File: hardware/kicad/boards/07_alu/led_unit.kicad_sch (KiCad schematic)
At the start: 120 parts

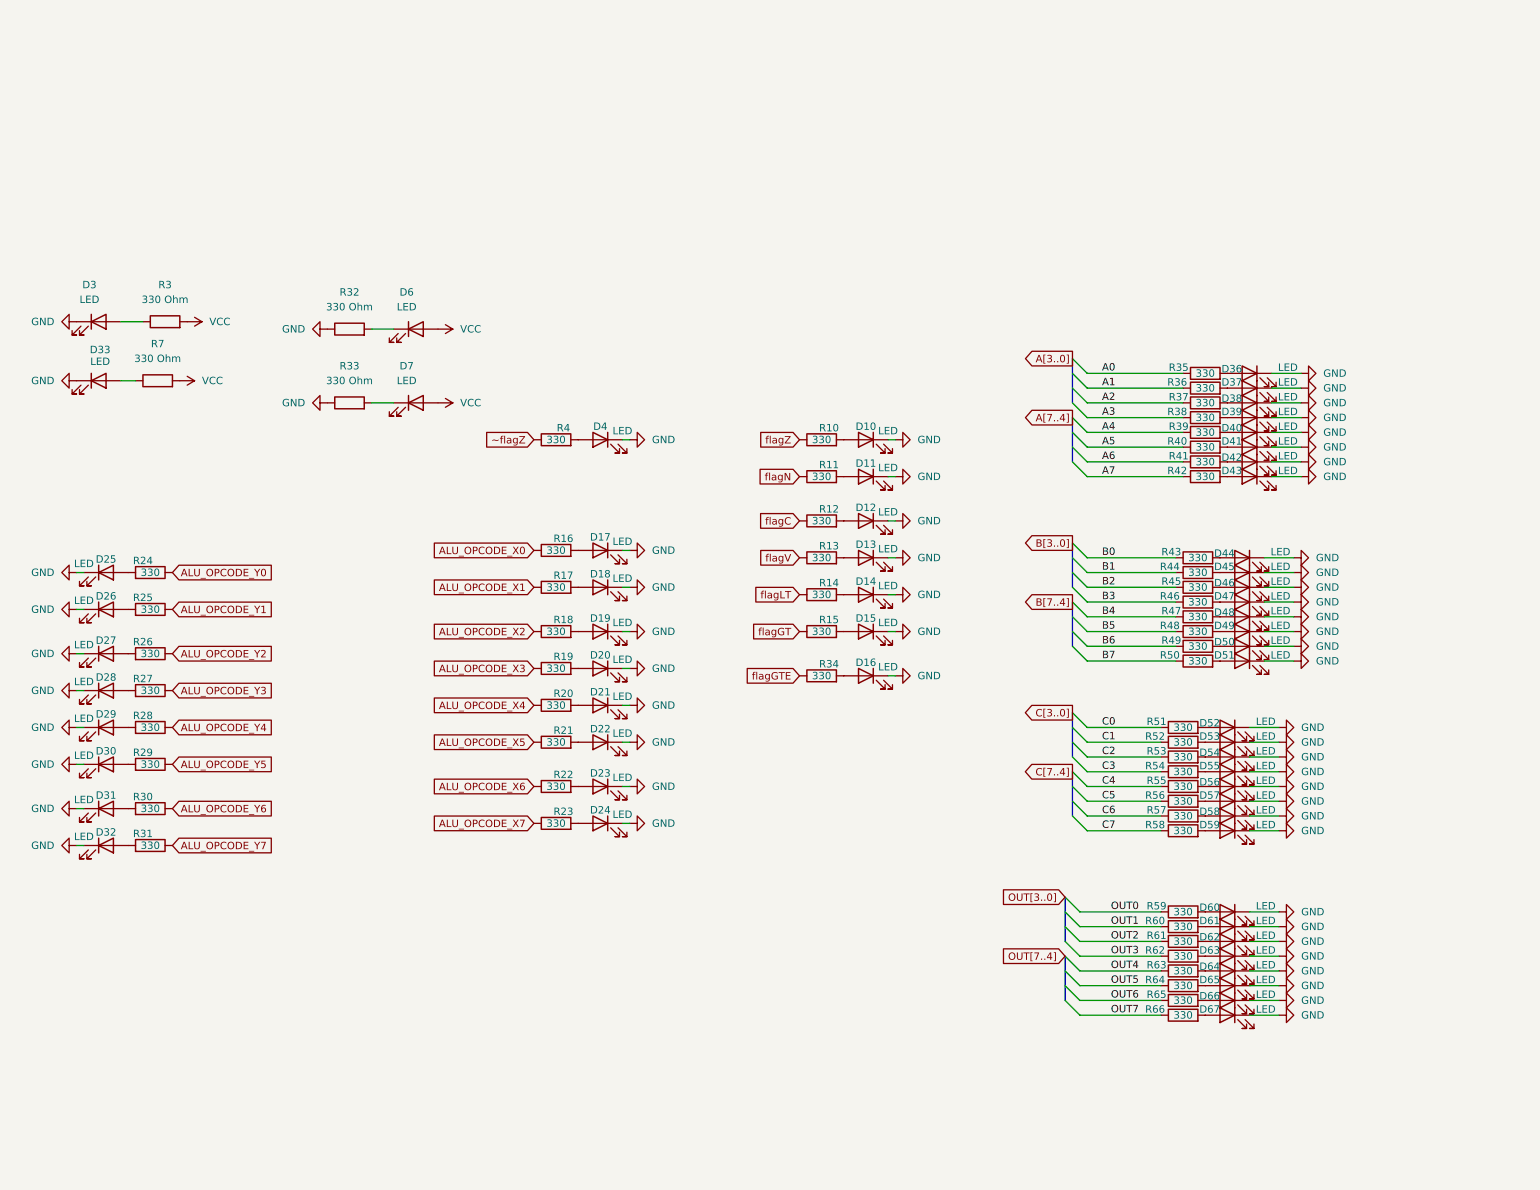
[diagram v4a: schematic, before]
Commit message: fix: replaced with resistor array/network over individual components
fix #5
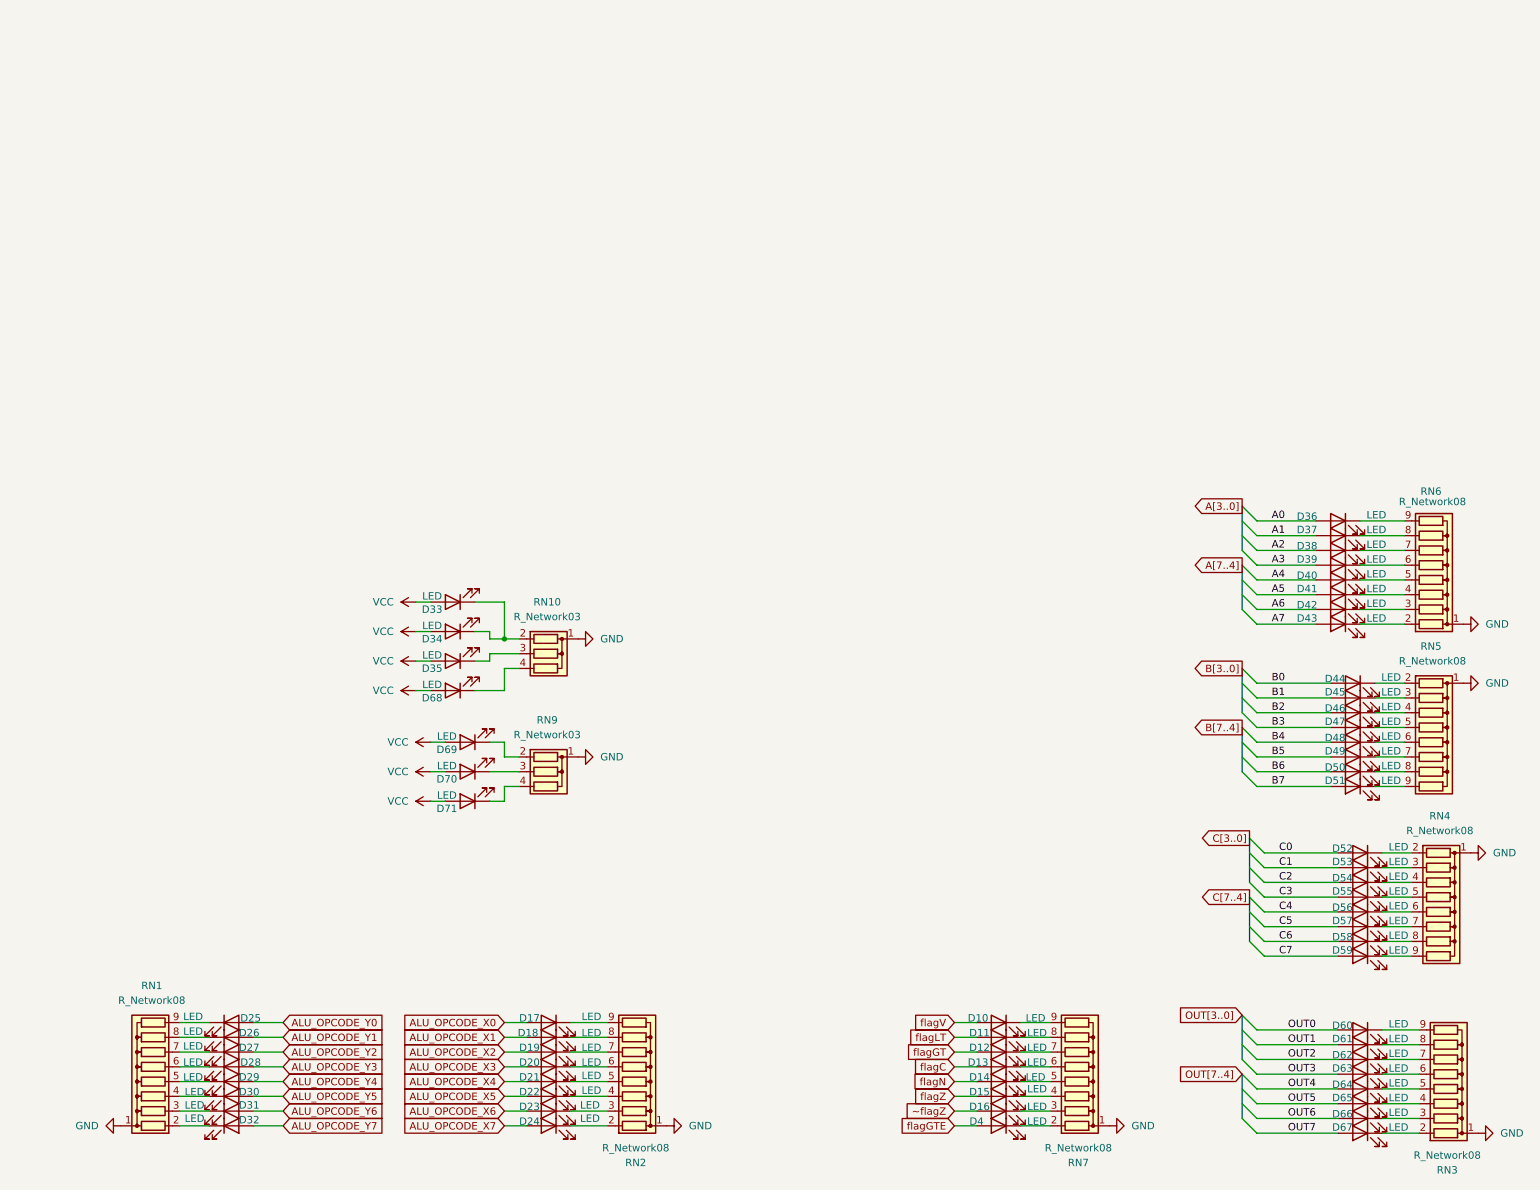
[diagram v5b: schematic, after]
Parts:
- removed D3, D6, D7: LED, LED_SMD:LED_0805_2012Metric, symbol Device:LED
- removed R10, R11, R12, R13, R14, R15, R16, R17, R18, R19, R20, R21, R22, R23, R24, R25, R26, R27, R28, R29, R30, R31, R34, R35, R36, R37, R38, R39, R4, R40, R41, R42, R43, R44, R45, R46, R47, R48, R49, R50, R51, R52, R53, R54, R55, R56, R57, R58, R59, R60, R61, R62, R63, R64, R65, R66: 330, Resistor_SMD:R_0603_1608Metric, symbol Device:R
- removed R3, R32, R33, R7: 330 Ohm, Resistor_SMD:R_0603_1608Metric, symbol Device:R
- added D34, D35, D68, D69, D70, D71: LED, LED_SMD:LED_0805_2012Metric, symbol Device:LED
- added RN1, RN2, RN3, RN4, RN5, RN6, RN7: R_Network08, Resistor_THT:R_Array_SIP9, symbol Device:R_Network08
- added RN10, RN9: R_Network03, Resistor_THT:R_Array_SIP4, symbol Device:R_Network03
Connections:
- net A0: now also D36.2 (A)
- net A1: now also D37.2 (A)
- net A2: now also D38.2 (A)
- net A3: now also D39.2 (A)
- net A4: now also D40.2 (A)
- net A5: now also D41.2 (A)
- net A6: now also D42.2 (A)
- net A7: now also D43.2 (A)
- net ALU_OPCODE_X0: now also D17.2 (A)
- net ALU_OPCODE_X1: now also D18.2 (A)
- net ALU_OPCODE_X2: now also D19.2 (A)
- net ALU_OPCODE_X3: now also D20.2 (A)
- net ALU_OPCODE_X4: now also D21.2 (A)
- net ALU_OPCODE_X5: now also D22.2 (A)
- net ALU_OPCODE_X6: now also D23.2 (A)
- net ALU_OPCODE_X7: now also D24.2 (A)
- net ALU_OPCODE_Y0: now also D25.2 (A)
- net ALU_OPCODE_Y1: now also D26.2 (A)
- net ALU_OPCODE_Y2: now also D27.2 (A)
- net ALU_OPCODE_Y3: now also D28.2 (A)
- net ALU_OPCODE_Y4: now also D29.2 (A)
- net ALU_OPCODE_Y5: now also D30.2 (A)
- net ALU_OPCODE_Y6: now also D31.2 (A)
- net ALU_OPCODE_Y7: now also D32.2 (A)
- net B0: now also D44.2 (A)
- net B1: now also D45.2 (A)
- net B2: now also D46.2 (A)
- net B3: now also D47.2 (A)
- net B4: now also D48.2 (A)
- net B5: now also D49.2 (A)
- net B6: now also D50.2 (A)
- net B7: now also D51.2 (A)
- net C0: now also D52.2 (A)
- net C1: now also D53.2 (A)
- net C2: now also D54.2 (A)
- net C3: now also D55.2 (A)
- net C4: now also D56.2 (A)
- net C5: now also D57.2 (A)
- net C6: now also D58.2 (A)
- net C7: now also D59.2 (A)
- net GND: now also RN1.1 (common), RN10.1 (common), RN2.1 (common), RN3.1 (common), RN4.1 (common), RN5.1 (common), RN6.1 (common), RN7.1 (common), RN9.1 (common); no longer D10.1 (K), D11.1 (K), D12.1 (K), D13.1 (K), D14.1 (K), D15.1 (K), D16.1 (K), D17.1 (K), D18.1 (K), D19.1 (K), D20.1 (K), D21.1 (K), D22.1 (K), D23.1 (K), D24.1 (K), D25.1 (K), D26.1 (K), D27.1 (K), D28.1 (K), D29.1 (K), D30.1 (K), D31.1 (K), D32.1 (K), D33.1 (K), D36.1 (K), D37.1 (K), D38.1 (K), D39.1 (K), D4.1 (K), D40.1 (K), D41.1 (K), D42.1 (K), D43.1 (K), D44.1 (K), D45.1 (K), D46.1 (K), D47.1 (K), D48.1 (K), D49.1 (K), D50.1 (K), D51.1 (K), D52.1 (K), D53.1 (K), D54.1 (K), D55.1 (K), D56.1 (K), D57.1 (K), D58.1 (K), D59.1 (K), D60.1 (K), D61.1 (K), D62.1 (K), D63.1 (K), D64.1 (K), D65.1 (K), D66.1 (K), D67.1 (K)
- net OUT0: now also D60.2 (A)
- net OUT1: now also D61.2 (A)
- net OUT2: now also D62.2 (A)
- net OUT3: now also D63.2 (A)
- net OUT4: now also D64.2 (A)
- net OUT5: now also D65.2 (A)
- net OUT6: now also D66.2 (A)
- net OUT7: now also D67.2 (A)
- net VCC: now also D33.2 (A), D34.2 (A), D35.2 (A), D68.2 (A), D69.2 (A), D70.2 (A), D71.2 (A)
- net flagC: now also D13.2 (A)
- net flagGT: now also D12.2 (A)
- net flagGTE: now also D4.2 (A)
- net flagLT: now also D11.2 (A)
- net flagN: now also D14.2 (A)
- net flagV: now also D10.2 (A)
- net flagZ: now also D15.2 (A)
- net ~flagZ: now also D16.2 (A)
- new net: D44.1 (K), RN5.2 (R1)
- new net: D52.1 (K), RN4.2 (R1)
- new net: D61.1 (K), RN3.8 (R7)
- new net: D16.1 (K), RN7.3 (R2)
- new net: D45.1 (K), RN5.3 (R2)
- new net: D46.1 (K), RN5.4 (R3)
- new net: D47.1 (K), RN5.5 (R4)
- new net: D48.1 (K), RN5.6 (R5)
- new net: D49.1 (K), RN5.7 (R6)
- new net: D50.1 (K), RN5.8 (R7)
- new net: D51.1 (K), RN5.9 (R8)
- new net: D59.1 (K), RN4.9 (R8)
- new net: D26.1 (K), RN1.8 (R7)
- new net: D63.1 (K), RN3.6 (R5)
- new net: D24.1 (K), RN2.2 (R1)
- new net: D23.1 (K), RN2.3 (R2)
- new net: D22.1 (K), RN2.4 (R3)
- new net: D21.1 (K), RN2.5 (R4)
- new net: D20.1 (K), RN2.6 (R5)
- new net: D19.1 (K), RN2.7 (R6)
- new net: D18.1 (K), RN2.8 (R7)
- new net: D17.1 (K), RN2.9 (R8)
- new net: D43.1 (K), RN6.2 (R1)
- new net: D42.1 (K), RN6.3 (R2)
- new net: D41.1 (K), RN6.4 (R3)
- new net: D40.1 (K), RN6.5 (R4)
- new net: D39.1 (K), RN6.6 (R5)
- new net: D38.1 (K), RN6.7 (R6)
- new net: D37.1 (K), RN6.8 (R7)
- new net: D36.1 (K), RN6.9 (R8)
- new net: D60.1 (K), RN3.9 (R8)
- new net: D28.1 (K), RN1.6 (R5)
- new net: D11.1 (K), RN7.8 (R7)
- new net: D69.1 (K), RN9.2 (R1)
- new net: D13.1 (K), RN7.6 (R5)
- new net: D54.1 (K), RN4.4 (R3)
- new net: D4.1 (K), RN7.2 (R1)
- new net: D15.1 (K), RN7.4 (R3)
- new net: D14.1 (K), RN7.5 (R4)
- new net: D12.1 (K), RN7.7 (R6)
- new net: D10.1 (K), RN7.9 (R8)
- new net: D29.1 (K), RN1.5 (R4)
- new net: D33.1 (K), D34.1 (K), RN10.2 (R1)
- new net: D35.1 (K), RN10.3 (R2)
- new net: D68.1 (K), RN10.4 (R3)
- new net: D65.1 (K), RN3.4 (R3)
- new net: D70.1 (K), RN9.3 (R2)
- new net: D32.1 (K), RN1.2 (R1)
- new net: D31.1 (K), RN1.3 (R2)
- new net: D30.1 (K), RN1.4 (R3)
- new net: D27.1 (K), RN1.7 (R6)
- new net: D25.1 (K), RN1.9 (R8)
- new net: D55.1 (K), RN4.5 (R4)
- new net: D62.1 (K), RN3.7 (R6)
- new net: D56.1 (K), RN4.6 (R5)
- new net: D58.1 (K), RN4.8 (R7)
- new net: D53.1 (K), RN4.3 (R2)
- new net: D66.1 (K), RN3.3 (R2)
- new net: D57.1 (K), RN4.7 (R6)
- new net: D64.1 (K), RN3.5 (R4)
- new net: D67.1 (K), RN3.2 (R1)
- new net: D71.1 (K), RN9.4 (R3)
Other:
- moved on the sheet: D10, D11, D12, D13, D14, D15, D16, D17, D18, D19, D20, D21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
